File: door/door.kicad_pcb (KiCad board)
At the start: 2 copper layers, 38.6 x 25.4 mm, 10 parts, among them J1 POWER, J2 CONTROL, J3 ENDPOINT, J4 MOTOR, Q1 IRF3205

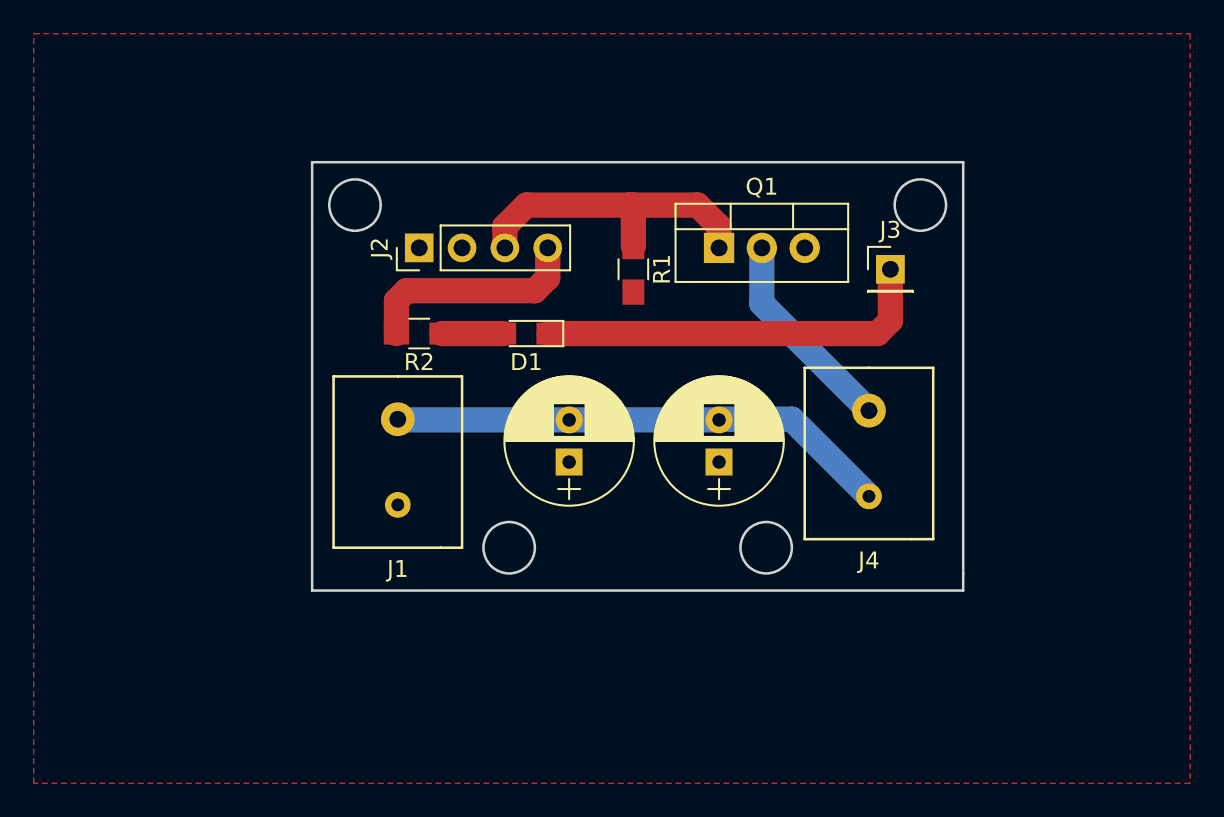
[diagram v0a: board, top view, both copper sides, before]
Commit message: Made the door pcb half the size
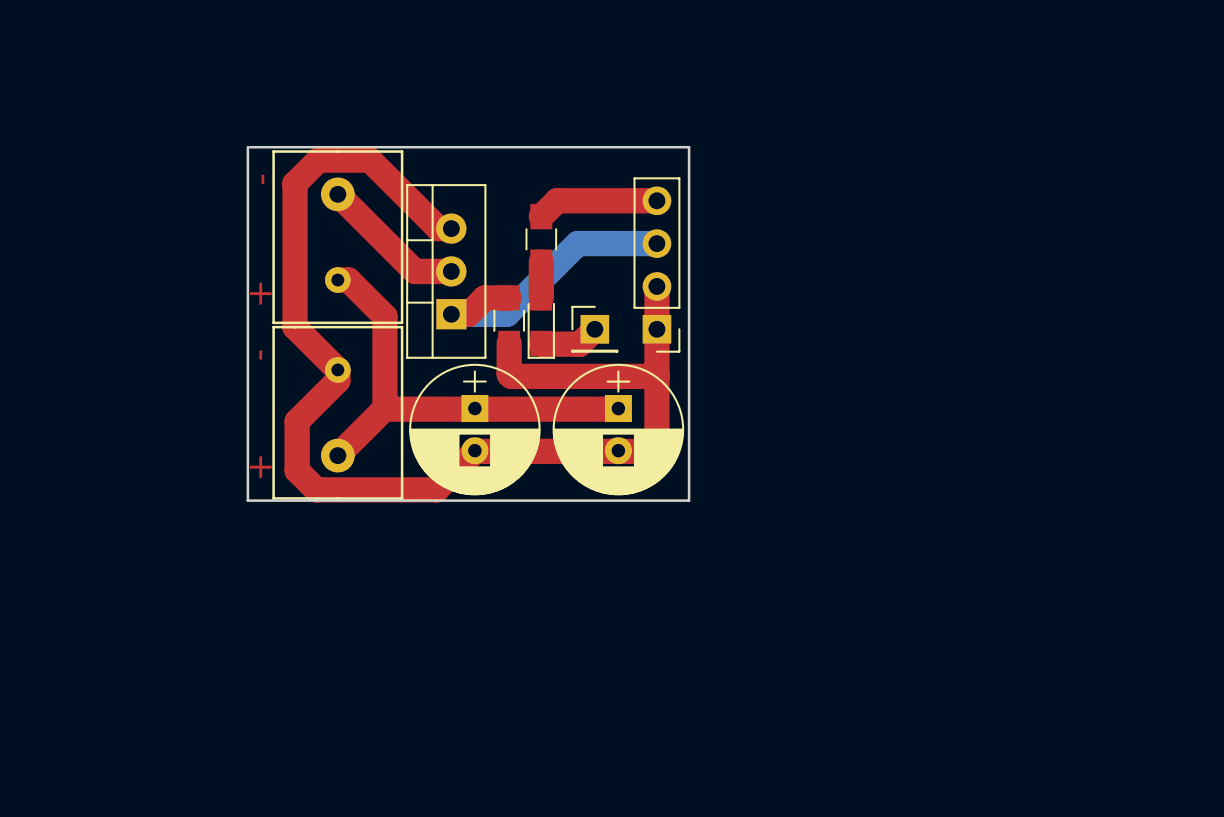
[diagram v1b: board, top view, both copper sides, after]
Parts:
- moved J4 34.0 mm to (133.6, 103.5)
- moved J3 17.9 mm to (148.8, 109.0)
- moved Q1 16.4 mm to (140.3, 108.1), turned to 90 degrees
- moved J2 14.9 mm to (152.5, 109.0), turned to 180 degrees
- moved R2 9.14 mm to (145.7, 103.6), turned to 90 degrees
- moved R1 7.97 mm to (143.8, 108.5)
- moved C1 6.76 mm to (150.2, 113.7), turned to 270 degrees
- moved C2 6.43 mm to (141.7, 113.7), turned to 270 degrees
- moved J1 4.60 mm to (133.6, 113.9), turned to 180 degrees
- moved D1 1.17 mm to (145.7, 108.5), turned to 90 degrees
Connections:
- C1 pad 1: GND -> +12V
- C1 pad 2: +12V -> GND
- C2 pad 1: GND -> +12V
- C2 pad 2: +12V -> GND
- J2 pad 1: Net-(J2-Pad1) -> GND
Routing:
- net GND: track 0.00 -> 73.3 mm
- net Net-(D1-Pad1): track 23.6 -> 3.56 mm
- net Net-(J2-Pad4): track 13.3 -> 7.25 mm
- net Net-(J4-Pad1): track 12.3 -> 8.62 mm
- net +12V: track 30.4 -> 27.0 mm
- net Net-(D1-Pad2): track 3.65 -> 2.13 mm
- net Net-(J2-Pad3): track 19.0 -> 17.8 mm
- removed copper zone on F.Cu, net GND
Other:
- board size 38.6 x 25.4 mm -> 26.2 x 21 mm
- net class 12V removed
- net class Default: trace_width 0.25 -> 1.5
- rule trace_min: 0.2 -> 1.5
- board text added: "+"
- board text added: "-"

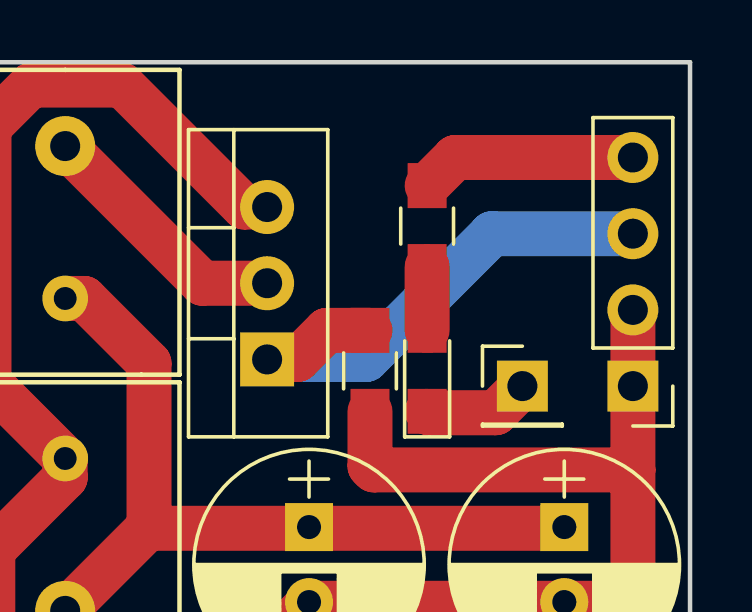
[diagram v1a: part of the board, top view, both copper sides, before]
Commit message: Added diode to the door signal
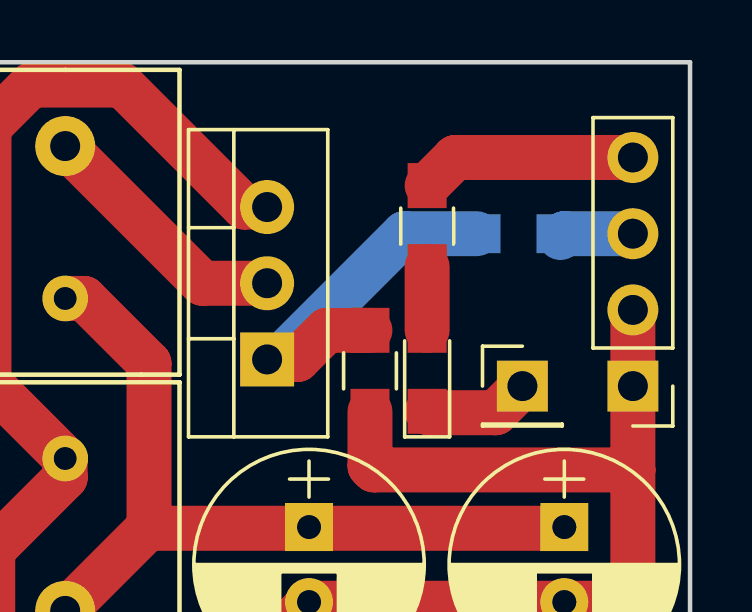
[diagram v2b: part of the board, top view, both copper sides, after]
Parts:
- added D2: D, Resistors_SMD:R_0805_HandSoldering, B.Cu at (148.7, 103.9)
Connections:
- J2 pad 3: Net-(J2-Pad3) -> Net-(D2-Pad2)
- Q1 pad 1: Net-(J2-Pad3) -> Net-(D2-Pad1)
- R1 pad 1: Net-(J2-Pad3) -> Net-(D2-Pad1)
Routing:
- net Net-(J2-Pad3): track 17.8 -> 0.00 mm
- net Net-(D2-Pad1): track 0.00 -> 12.6 mm
- net Net-(D2-Pad2): track 0.00 -> 2.47 mm
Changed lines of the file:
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@@
 (kicad_pcb (version 4) (host pcbnew 4.0.6)
   (general
-    (links 15)
+    (links 16)
     (no_connects 0)
     (area 128.194999 98.095999 154.507001 119.201001)
     (thickness 1.6)
     (drawings 11)
-    (tracks 42)
+    (tracks 44)
     (zones 0)
-    (modules 10)
-    (nets 8)
+    (modules 11)
+    (nets 9)
   )
   (page A4)
@@
   (net 3 "Net-(D1-Pad1)")
   (net 4 "Net-(D1-Pad2)")
-  (net 5 "Net-(J2-Pad3)")
-  (net 6 "Net-(J2-Pad4)")
-  (net 7 "Net-(J4-Pad1)")
+  (net 5 "Net-(J2-Pad4)")
+  (net 6 "Net-(J4-Pad1)")
+  (net 7 "Net-(D2-Pad1)")
+  (net 8 "Net-(D2-Pad2)")
   (net_class Default "This is the default net class."
     (clearance 0.2)
@@
     (add_net "Net-(D1-Pad1)")
     (add_net "Net-(D1-Pad2)")
-    (add_net "Net-(J2-Pad3)")
+    (add_net "Net-(D2-Pad1)")
+    (add_net "Net-(D2-Pad2)")
     (add_net "Net-(J2-Pad4)")
     (add_net "Net-(J4-Pad1)")
@@
       (net 1 GND))
     (pad 3 thru_hole oval (at 0 5.08 180) (size 1.7 1.7) (drill 1) (layers *.Cu *.Mask)
-      (net 5 "Net-(J2-Pad3)"))
+      (net 8 "Net-(D2-Pad2)"))
     (pad 4 thru_hole oval (at 0 7.62 180) (size 1.7 1.7) (drill 1) (layers *.Cu *.Mask)
-      (net 6 "Net-(J2-Pad4)"))
+      (net 5 "Net-(J2-Pad4)"))
     (model ${KISYS3DMOD}/Pin_Headers.3dshapes/Pin_Header_Straight_1x04_Pitch2.54mm.wrl
       (at (xyz 0 0 0))
@@
     (fp_line (start 3.81 -5.08) (end 0 -5.08) (layer F.SilkS) (width 0.15))
     (pad 1 thru_hole circle (at 0 -2.54) (size 2 2) (drill 1) (layers *.Cu *.Mask)
-      (net 7 "Net-(J4-Pad1)"))
+      (net 6 "Net-(J4-Pad1)"))
     (pad 2 thru_hole circle (at 0 2.54) (size 1.524 1.524) (drill 0.762) (layers *.Cu *.Mask)
       (net 2 +12V))
@@
     (fp_line (start 7.79 -2.75) (end -2.71 -2.75) (layer F.CrtYd) (width 0.05))
     (pad 1 thru_hole rect (at 0 0 90) (size 1.8 1.8) (drill 1) (layers *.Cu *.Mask)
-      (net 5 "Net-(J2-Pad3)"))
+      (net 7 "Net-(D2-Pad1)"))
     (pad 2 thru_hole oval (at 2.54 0 90) (size 1.8 1.8) (drill 1) (layers *.Cu *.Mask)
-      (net 7 "Net-(J4-Pad1)"))
+      (net 6 "Net-(J4-Pad1)"))
     (pad 3 thru_hole oval (at 5.08 0 90) (size 1.8 1.8) (drill 1) (layers *.Cu *.Mask)
       (net 1 GND))
@@
     (fp_line (start 2.35 0.9) (end -2.35 0.9) (layer F.CrtYd) (width 0.05))
     (pad 1 smd rect (at -1.35 0 270) (size 1.5 1.3) (layers F.Cu F.Paste F.Mask)
-      (net 5 "Net-(J2-Pad3)"))
+      (net 7 "Net-(D2-Pad1)"))
     (pad 2 smd rect (at 1.35 0 270) (size 1.5 1.3) (layers F.Cu F.Paste F.Mask)
       (net 1 GND))
@@
       (net 4 "Net-(D1-Pad2)"))
     (pad 2 smd rect (at 1.35 0 90) (size 1.5 1.3) (layers F.Cu F.Paste F.Mask)
-      (net 6 "Net-(J2-Pad4)"))
+      (net 5 "Net-(J2-Pad4)"))
+    (model ${KISYS3DMOD}/Resistors_SMD.3dshapes/R_0805.wrl
+      (at (xyz 0 0 0))
+      (scale (xyz 1 1 1))
+      (rotate (xyz 0 0 0))
+    )
+  )
+  (module Resistors_SMD:R_0805_HandSoldering (layer B.Cu)
+    (at 148.717 103.886)
+    (descr "Resistor SMD 0805, hand soldering")
+    (tags "resistor 0805")
+    (attr smd)
+    (fp_text reference D2 (at 0 1.7) (layer B.SilkS) hide
+      (effects (font (size 1 1) (thickness 0.15)) (justify mirror))
+    )
+    (fp_text value D (at 0 -1.75) (layer B.Fab) hide
+      (effects (font (size 1 1) (thickness 0.15)) (justify mirror))
+    )
+    (fp_text user %R (at 0 0) (layer B.Fab) hide
+      (effects (font (size 0.5 0.5) (thickness 0.075)) (justify mirror))
+    )
+    (fp_line (start -1 -0.62) (end -1 0.62) (layer B.Fab) (width 0.1))
+    (fp_line (start 1 -0.62) (end -1 -0.62) (layer B.Fab) (width 0.1))
+    (fp_line (start 1 0.62) (end 1 -0.62) (layer B.Fab) (width 0.1))
+    (fp_line (start -1 0.62) (end 1 0.62) (layer B.Fab) (width 0.1))
+    (fp_line (start 0.6 -0.88) (end -0.6 -0.88) (layer B.SilkS) (width 0.12))
+    (fp_line (start -0.6 0.88) (end 0.6 0.88) (layer B.SilkS) (width 0.12))
+    (fp_line (start -2.35 0.9) (end 2.35 0.9) (layer B.CrtYd) (width 0.05))
+    (fp_line (start -2.35 0.9) (end -2.35 -0.9) (layer B.CrtYd) (width 0.05))
+    (fp_line (start 2.35 -0.9) (end 2.35 0.9) (layer B.CrtYd) (width 0.05))
+    (fp_line (start 2.35 -0.9) (end -2.35 -0.9) (layer B.CrtYd) (width 0.05))
+    (pad 1 smd rect (at -1.35 0) (size 1.5 1.3) (layers B.Cu B.Paste B.Mask)
+      (net 7 "Net-(D2-Pad1)"))
+    (pad 2 smd rect (at 1.35 0) (size 1.5 1.3) (layers B.Cu B.Paste B.Mask)
+      (net 8 "Net-(D2-Pad2)"))
     (model ${KISYS3DMOD}/Resistors_SMD.3dshapes/R_0805.wrl
       (at (xyz 0 0 0))
@@
   (segment (start 145.716 109.855) (end 145.669 109.808) (width 1.5) (layer F.Cu) (net 3))
   (segment (start 145.669 104.982) (end 145.669 107.108) (width 1.5) (layer F.Cu) (net 4))
-  (segment (start 140.335 108.077) (end 141.351 108.077) (width 1.5) (layer F.Cu) (net 5))
-  (segment (start 142.32 107.108) (end 143.764 107.108) (width 1.5) (layer F.Cu) (net 5))
-  (segment (start 141.351 108.077) (end 142.32 107.108) (width 1.5) (layer F.Cu) (net 5))
-  (segment (start 152.527 103.886) (end 147.828 103.886) (width 1.5) (layer B.Cu) (net 5))
-  (segment (start 143.637 108.077) (end 140.335 108.077) (width 1.5) (layer B.Cu) (net 5))
-  (segment (start 147.828 103.886) (end 143.637 108.077) (width 1.5) (layer B.Cu) (net 5))
-  (segment (start 152.527 101.346) (end 146.605 101.346) (width 1.5) (layer F.Cu) (net 6))
-  (segment (start 146.605 101.346) (end 145.669 102.282) (width 1.5) (layer F.Cu) (net 6))
-  (segment (start 140.335 105.537) (end 138.176 105.537) (width 1.5) (layer F.Cu) (net 7))
-  (segment (start 138.176 105.537) (end 133.604 100.965) (width 1.5) (layer F.Cu) (net 7))
+  (segment (start 152.527 101.346) (end 146.605 101.346) (width 1.5) (layer F.Cu) (net 5))
+  (segment (start 146.605 101.346) (end 145.669 102.282) (width 1.5) (layer F.Cu) (net 5))
+  (segment (start 140.335 105.537) (end 138.176 105.537) (width 1.5) (layer F.Cu) (net 6))
+  (segment (start 138.176 105.537) (end 133.604 100.965) (width 1.5) (layer F.Cu) (net 6))
+  (segment (start 140.335 108.077) (end 140.716 108.077) (width 1.5) (layer B.Cu) (net 7))
+  (segment (start 140.716 108.077) (end 144.907 103.886) (width 1.5) (layer B.Cu) (net 7))
+  (segment (start 144.907 103.886) (end 147.32 103.886) (width 1.5) (layer B.Cu) (net 7))
+  (segment (start 140.335 108.077) (end 141.351 108.077) (width 1.5) (layer F.Cu) (net 7))
+  (segment (start 142.32 107.108) (end 143.764 107.108) (width 1.5) (layer F.Cu) (net 7))
+  (segment (start 141.351 108.077) (end 142.32 107.108) (width 1.5) (layer F.Cu) (net 7))
+  (segment (start 152.527 103.886) (end 150.241 103.886) (width 1.5) (layer B.Cu) (net 8))
+  (segment (start 150.241 103.886) (end 150.114 104.013) (width 1.5) (layer B.Cu) (net 8))
 )

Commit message: Fixed text layers
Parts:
- moved J3 0.38 mm to (149.2, 109.0)
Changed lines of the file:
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@@
     (links 16)
     (no_connects 0)
-    (area 128.194999 98.095999 154.507001 119.201001)
+    (area 127.705 97.982999 157.92 119.441002)
     (thickness 1.6)
     (drawings 11)
@@
     (fp_line (start 5.35 4.1) (end 5.35 -4.1) (layer F.CrtYd) (width 0.05))
     (fp_line (start 5.35 -4.1) (end -2.85 -4.1) (layer F.CrtYd) (width 0.05))
-    (fp_text user %R (at 1.25 0 270) (layer F.Fab)
+    (fp_text user %R (at 1.25 0 270) (layer F.Fab) hide
       (effects (font (size 1 1) (thickness 0.15)))
     )
@@
     (fp_line (start 5.35 4.1) (end 5.35 -4.1) (layer F.CrtYd) (width 0.05))
     (fp_line (start 5.35 -4.1) (end -2.85 -4.1) (layer F.CrtYd) (width 0.05))
-    (fp_text user %R (at 1.25 0 270) (layer F.Fab)
+    (fp_text user %R (at 1.25 0 270) (layer F.Fab) hide
       (effects (font (size 1 1) (thickness 0.15)))
     )
@@
       (effects (font (size 1 1) (thickness 0.15)))
     )
-    (fp_text value LED (at -0.381 1.397 90) (layer F.Fab)
-      (effects (font (size 0.6 1) (thickness 0.15)))
+    (fp_text value LED (at -0.381 1.524 90) (layer F.SilkS)
+      (effects (font (size 1 1) (thickness 0.15)))
     )
     (fp_line (start -0.4 -0.4) (end -0.4 0.4) (layer F.Fab) (width 0.1))
@@
       (effects (font (size 1 1) (thickness 0.15)))
     )
-    (fp_text value POWER (at 4.572 0 450) (layer F.Fab)
+    (fp_text value POWER (at 4.572 0 270) (layer F.SilkS)
       (effects (font (size 1 1) (thickness 0.15)))
     )
@@
   )
   (module Pin_Headers:Pin_Header_Straight_1x01_Pitch2.54mm (layer F.Cu)
-    (at 148.844 108.966)
+    (at 149.225 108.966)
     (descr "Through hole straight pin header, 1x01, 2.54mm pitch, single row")
     (tags "Through hole pin header THT 1x01 2.54mm single row")
@@
     (fp_line (start 1.8 1.8) (end 1.8 -1.8) (layer F.CrtYd) (width 0.05))
     (fp_line (start 1.8 -1.8) (end -1.8 -1.8) (layer F.CrtYd) (width 0.05))
-    (fp_text user %R (at 0 0 90) (layer F.Fab)
+    (fp_text user %R (at 0 0 90) (layer F.Fab) hide
       (effects (font (size 1 1) (thickness 0.15)))
     )
@@
       (effects (font (size 1 1) (thickness 0.15)))
     )
-    (fp_text value MOTOR (at -4.572 0 90) (layer F.Fab)
+    (fp_text value MOTOR (at -4.572 0 90) (layer F.SilkS)
       (effects (font (size 1 1) (thickness 0.15)))
     )
@@
       (effects (font (size 1 1) (thickness 0.15)))
     )
-    (fp_text value "R 3K" (at -4.318 0 270) (layer F.Fab)
+    (fp_text value "R 3K" (at -4.318 0 270) (layer F.SilkS)
       (effects (font (size 1 1) (thickness 0.15)))
     )
@@
       (effects (font (size 1 1) (thickness 0.15)))
     )
-    (fp_text value "R 330" (at 0 1.651 90) (layer F.Fab)
+    (fp_text value "R 330" (at 0 1.651 90) (layer F.SilkS)
       (effects (font (size 1 1) (thickness 0.15)))
     )
@@
   (gr_line (start 154.432 98.171) (end 154.432 119.126) (angle 90) (layer Edge.Cuts) (width 0.15))
   (gr_line (start 128.397 98.171) (end 154.432 98.171) (angle 90) (layer Edge.Cuts) (width 0.15))
-  (gr_text - (at 129.032 100.076 90) (layer F.Cu)
+  (gr_text - (at 129.032 100.076 90) (layer F.SilkS)
     (effects (font (size 1.5 1.5) (thickness 0.3)))
   )
-  (gr_text - (at 128.905 110.49 90) (layer F.Cu)
+  (gr_text - (at 128.905 110.49 90) (layer F.SilkS)
     (effects (font (size 1.5 1.5) (thickness 0.3)))
   )
-  (gr_text + (at 129.032 117.094) (layer F.Cu)
+  (gr_text + (at 129.032 117.094) (layer F.SilkS)
     (effects (font (size 1.5 1.5) (thickness 0.3)))
   )
-  (gr_text + (at 129.032 106.807) (layer F.Cu)
+  (gr_text + (at 129.032 106.807) (layer F.SilkS)
     (effects (font (size 1.5 1.5) (thickness 0.3)))
   )
-  (gr_text C (at 149.606 101.346 90) (layer F.Fab)
+  (gr_text C (at 149.606 101.346 90) (layer F.SilkS)
     (effects (font (size 1.5 1.5) (thickness 0.3)))
   )
-  (gr_text S (at 149.733 103.886 90) (layer F.Fab)
+  (gr_text S (at 149.733 103.886 90) (layer F.SilkS)
     (effects (font (size 1.5 1.5) (thickness 0.3)))
   )
-  (gr_text G (at 149.733 106.172 90) (layer F.Fab)
+  (gr_text G (at 149.733 106.172 90) (layer F.SilkS)
     (effects (font (size 1.5 1.5) (thickness 0.3)))
   )

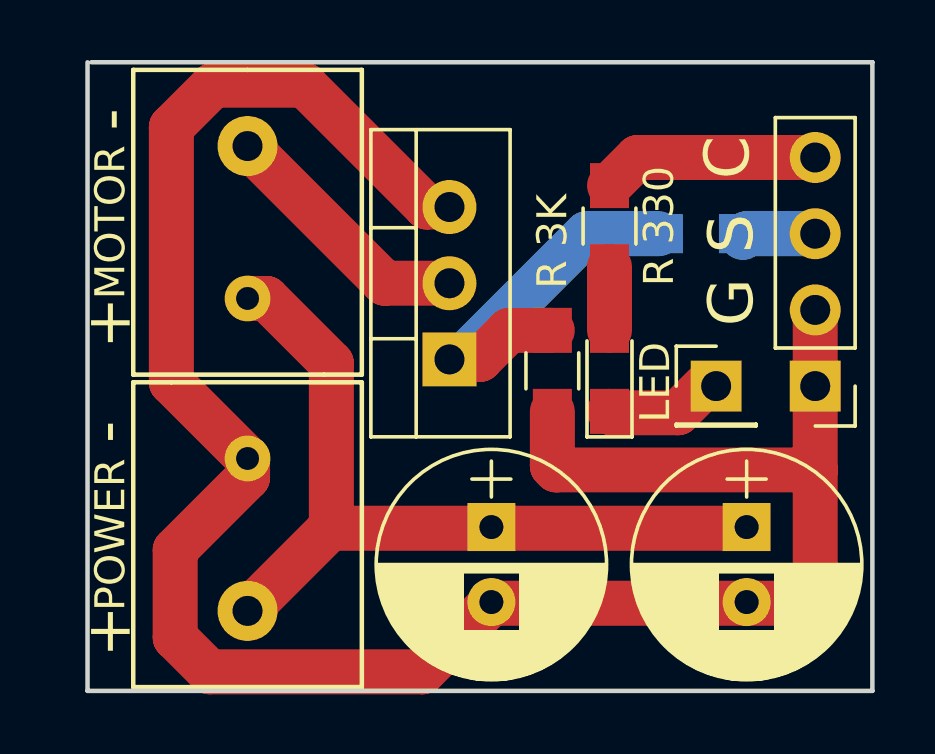
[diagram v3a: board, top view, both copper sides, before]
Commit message: Updated screw terminal footprint and moved components around
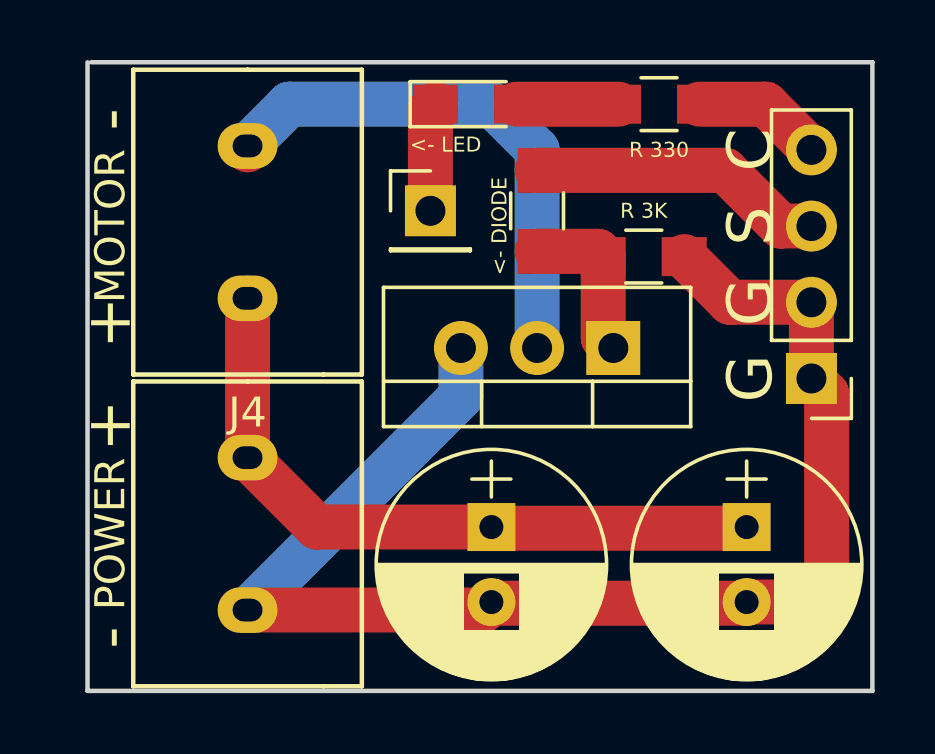
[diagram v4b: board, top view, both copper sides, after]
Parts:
- D1: value LED -> <- LED
- D2: moved to F.Cu
- moved J3 11.2 mm to (139.7, 103.1)
- moved D1 9.94 mm to (141.2, 99.6), turned to 0 degrees
- moved D2 5.51 mm to (143.3, 103.1), turned to 90 degrees
- moved Q1 5.47 mm to (145.8, 107.7), turned to 180 degrees
- moved R1 4.88 mm to (146.8, 104.6), turned to 0 degrees
- moved R2 4.39 mm to (147.3, 99.6), turned to 0 degrees
- moved J2 0.28 mm to (152.4, 108.7)
- turned J1 to 0 degrees
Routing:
- net GND: track 73.3 -> 46.0 mm
- net Net-(J4-Pad1): track 8.62 -> 17.6 mm
- net Net-(D2-Pad2): track 2.47 -> 9.91 mm
- net Net-(D2-Pad1): track 12.6 -> 5.46 mm
- net +12V: track 27.0 -> 22.9 mm
- net Net-(J2-Pad4): track 7.25 -> 4.36 mm
- net Net-(D1-Pad2): track 2.13 -> 3.40 mm
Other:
- board text added: "<- DIODE"
